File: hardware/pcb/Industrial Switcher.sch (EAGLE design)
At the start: 59 parts, among them IC1 MSP430FR5739, IC2 HY-TFT220, Q1 IRFR5305, Q2 32 kHz, Q3 IRFZ34NS, Q4 IRFZ34NS, Q5 IRFZ34NS, Q6 IRFZ34NS, U1 TDA3664, U2 TPS76933, U3 LT1161CSWPBF

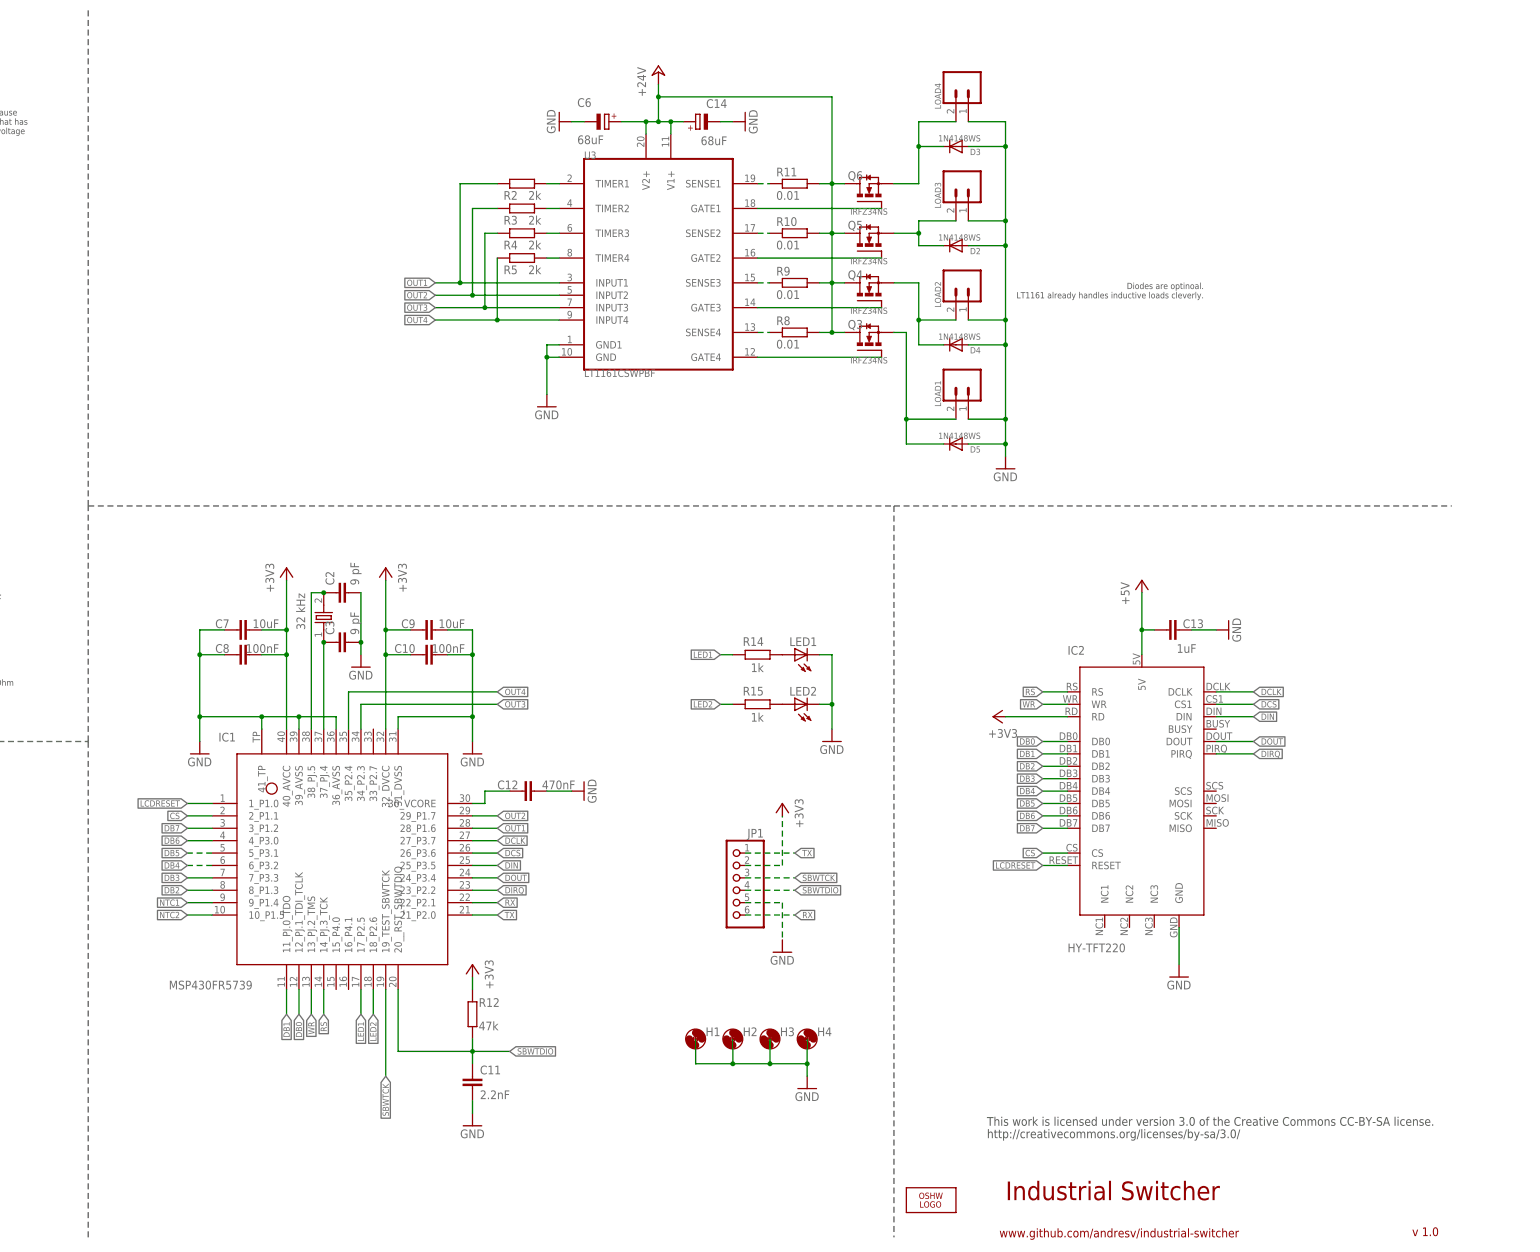
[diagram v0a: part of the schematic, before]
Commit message: Separated digital and power groundplane.
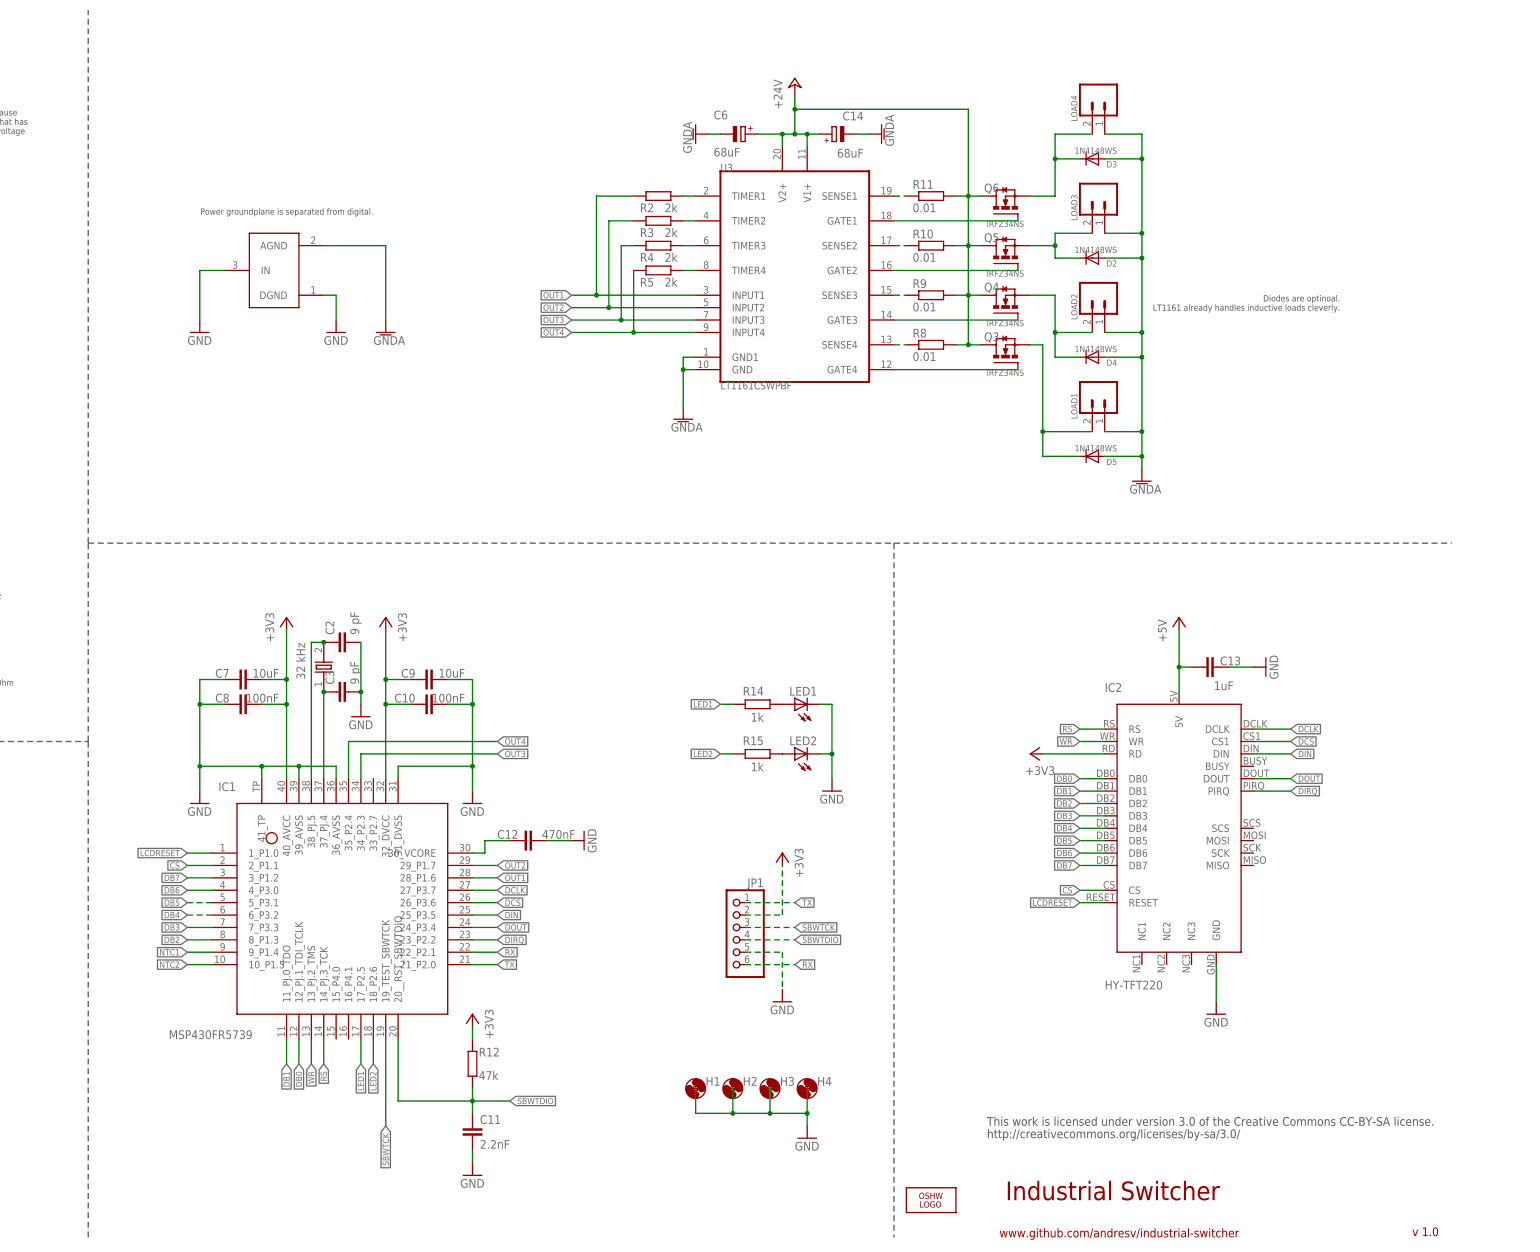
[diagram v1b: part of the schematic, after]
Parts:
- added U$1: GND_CONNECT, SparkFun-Passives:GND_CONNECT
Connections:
- new net GNDA: C14.-, C6.-, D2.A, D3.A, D4.A, D5.A, LOAD1.1, LOAD2.1, LOAD3.1, LOAD4.1, U$1.AGND, U3.GND, U3.GND1
- net GND: now also U$1.DGND, U$1.IN; no longer C14.-, C6.-, D2.A, D3.A, D4.A, D5.A, LOAD1.1, LOAD2.1, LOAD3.1, LOAD4.1, U3.GND, U3.GND1
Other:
- note added: "Power groundplane is separated from digital."
- moved on the sheet: C10, C11, C12, C13, C14, C2, C3, C6, C7, C8, C9, D2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

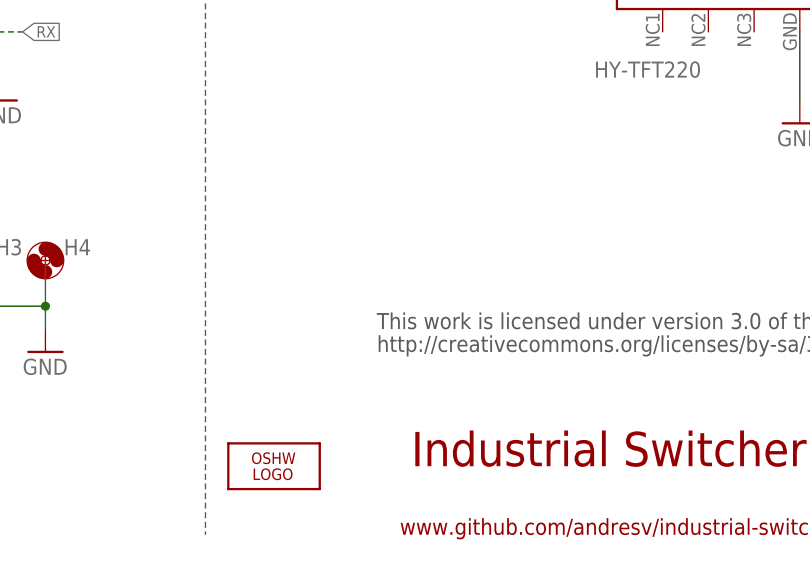
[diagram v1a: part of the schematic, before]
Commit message: Replaced OSHW logo.
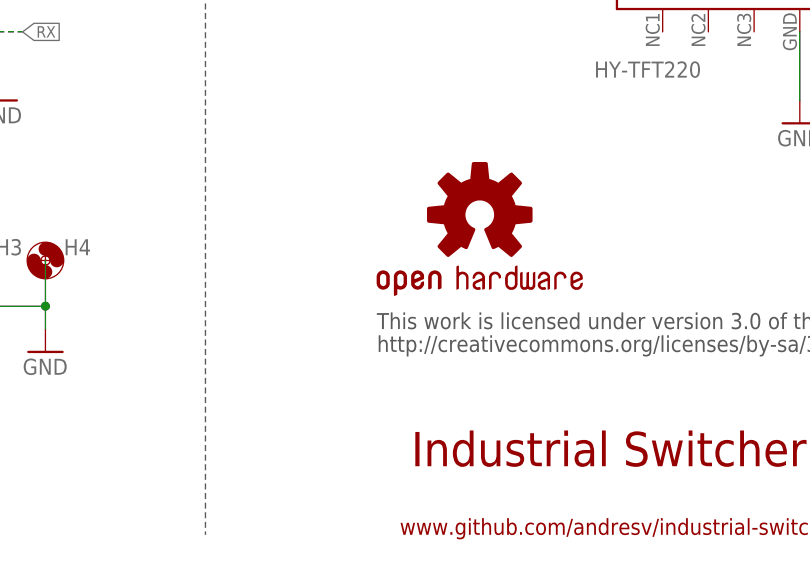
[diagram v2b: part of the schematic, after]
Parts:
- removed LOGO1: OSHW_LOGO_8MILX0350-NT, OSHW:OSHW_LOGO_8MILX0350-NT
- added LOGO2: OSHW-LOGOL, SparkFun-Aesthetics:OSHW-LOGOL
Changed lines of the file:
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@@
 <setting verticaltext="up"/>
 </settings>
-<grid distance="0.1" unitdist="inch" unit="inch" style="lines" multiple="1" display="yes" altdistance="0.01" altunitdist="inch" altunit="inch"/>
+<grid distance="0.1" unitdist="inch" unit="inch" style="lines" multiple="1" display="no" altdistance="0.01" altunitdist="inch" altunit="inch"/>
 <layers>
 <layer number="1" name="Top" color="4" fill="1" visible="no" active="no"/>
@@
 <parts>
 <part name="FRAME1" library="frames" deviceset="A3L-LOC" device=""/>
-<part name="LOGO1" library="OSHW" deviceset="OSHW_LOGO_8MIL" device="X0350-NT"/>
 <part name="NTC2" library="ptc-ntc" deviceset="NTC640-9" device="" value="4k7"/>
 <part name="GND10" library="supply1" deviceset="GND" device=""/>
@@
 <part name="GND26" library="supply1" deviceset="GND" device=""/>
 <part name="GND8" library="supply1" deviceset="GNDA" device=""/>
+<part name="LOGO2" library="SparkFun-Aesthetics" deviceset="OSHW-LOGO" device="L" value="OSHW-LOGOL"/>
 </parts>
 <sheets>
@@
 <instances>
 <instance part="FRAME1" gate="G$1" x="0" y="0"/>
-<instance part="LOGO1" gate="G$1" x="276.86" y="12.7"/>
 <instance part="NTC2" gate="1" x="66.04" y="50.8"/>
 <instance part="GND10" gate="1" x="66.04" y="40.64"/>
@@
 <attribute name="VALUE" x="223.52" y="170.18" size="1.778" layer="96"/>
 </instance>
+<instance part="LOGO2" gate="G$1" x="299.72" y="40.64"/>
 </instances>
 <busses>
